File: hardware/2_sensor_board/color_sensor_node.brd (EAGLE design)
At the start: 27.9 x 30.5 mm, 19 parts, among them J1 JTAG, J2 JTAG, U1 ISL29125, U2 3.3V, U3 WS2811

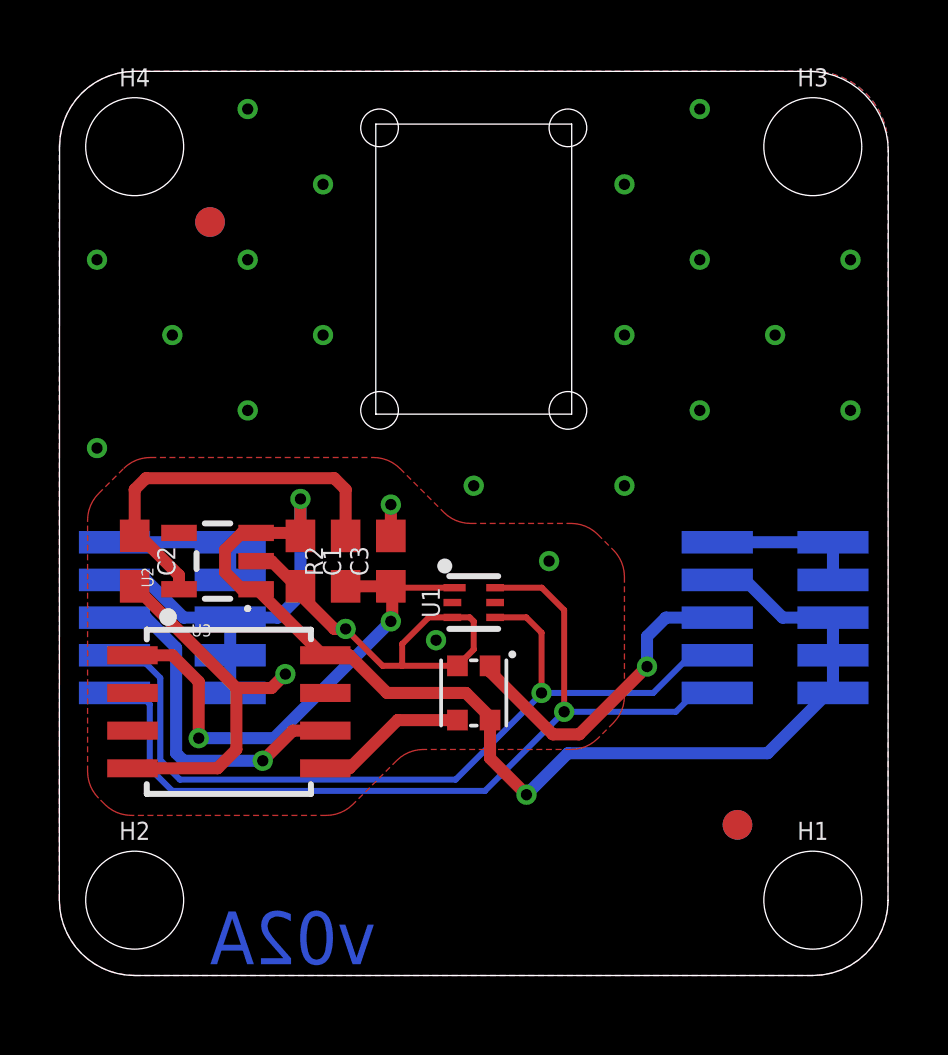
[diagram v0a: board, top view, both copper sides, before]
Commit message: increase standoff size sensor board
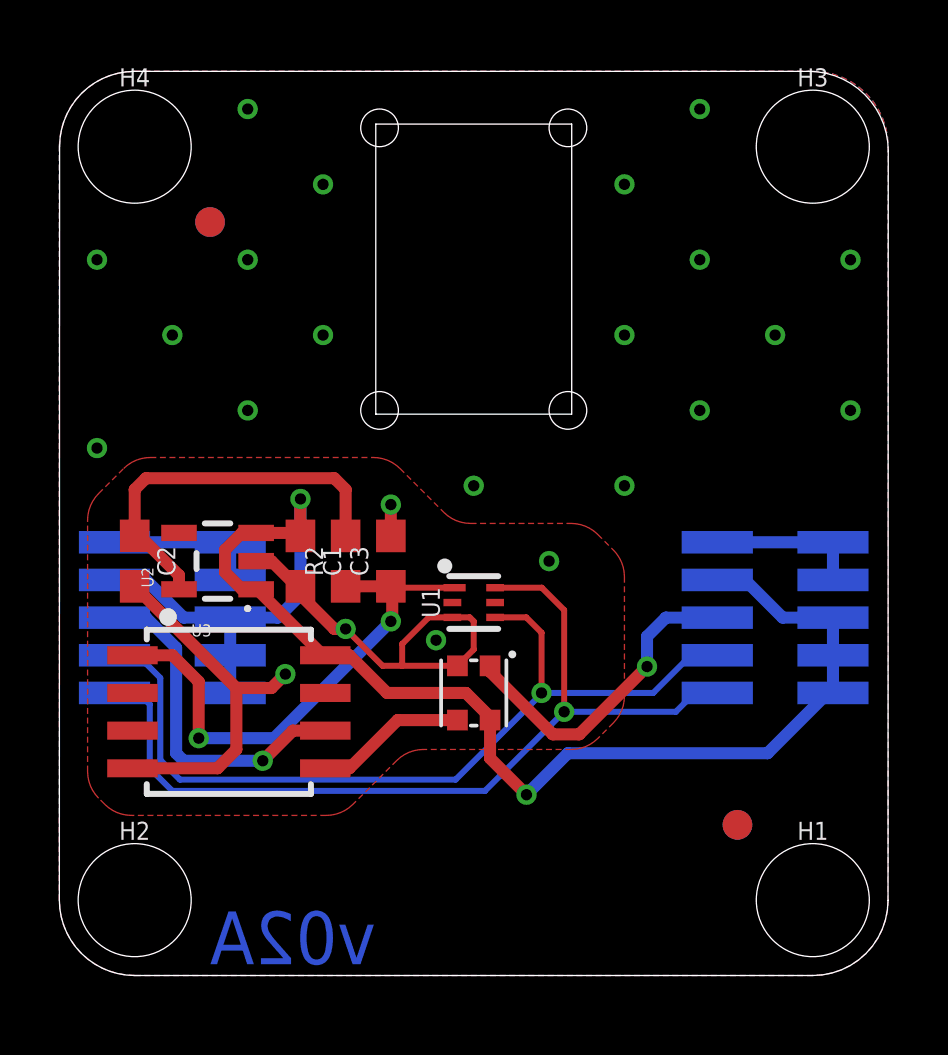
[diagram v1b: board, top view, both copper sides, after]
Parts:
- H1, H2, H3, H4: value STAND-OFF -> STAND-OFF#8; device SparkFun-Hardware:STAND-OFF -> standoff:STAND-OFF-#8
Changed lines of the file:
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@@
 <drawing>
 <settings>
-<setting alwaysvectorfont="yes"/>
+<setting alwaysvectorfont="no"/>
 <setting verticaltext="up"/>
 </settings>
-<grid distance="50" unitdist="mil" unit="mil" style="lines" multiple="1" display="yes" altdistance="1" altunitdist="mil" altunit="mil"/>
+<grid distance="5" unitdist="mil" unit="mil" style="lines" multiple="1" display="yes" altdistance="5" altunitdist="mil" altunit="mil"/>
 <layers>
 <layer number="1" name="Top" color="4" fill="1" visible="yes" active="yes"/>
-<layer number="16" name="Bottom" color="1" fill="1" visible="no" active="yes"/>
+<layer number="16" name="Bottom" color="1" fill="1" visible="yes" active="yes"/>
 <layer number="17" name="Pads" color="2" fill="1" visible="yes" active="yes"/>
 <layer number="18" name="Vias" color="2" fill="1" visible="yes" active="yes"/>
@@
 <layer number="20" name="Dimension" color="24" fill="1" visible="yes" active="yes"/>
 <layer number="21" name="tPlace" color="16" fill="1" visible="yes" active="yes"/>
-<layer number="22" name="bPlace" color="14" fill="1" visible="no" active="yes"/>
+<layer number="22" name="bPlace" color="14" fill="1" visible="yes" active="yes"/>
 <layer number="23" name="tOrigins" color="15" fill="1" visible="yes" active="yes"/>
-<layer number="24" name="bOrigins" color="15" fill="1" visible="no" active="yes"/>
-<layer number="25" name="tNames" color="7" fill="1" visible="yes" active="yes"/>
+<layer number="24" name="bOrigins" color="15" fill="1" visible="yes" active="yes"/>
+<layer number="25" name="tNames" color="7" fill="1" visible="no" active="yes"/>
 <layer number="26" name="bNames" color="7" fill="1" visible="no" active="yes"/>
 <layer number="27" name="tValues" color="7" fill="1" visible="no" active="yes"/>
@@
 <layer number="37" name="tTest" color="7" fill="1" visible="no" active="yes"/>
 <layer number="38" name="bTest" color="7" fill="1" visible="no" active="yes"/>
-<layer number="39" name="tKeepout" color="4" fill="11" visible="yes" active="yes"/>
+<layer number="39" name="tKeepout" color="4" fill="11" visible="no" active="yes"/>
 <layer number="40" name="bKeepout" color="1" fill="11" visible="no" active="yes"/>
-<layer number="41" name="tRestrict" color="4" fill="10" visible="yes" active="yes"/>
+<layer number="41" name="tRestrict" color="4" fill="10" visible="no" active="yes"/>
 <layer number="42" name="bRestrict" color="1" fill="10" visible="no" active="yes"/>
 <layer number="43" name="vRestrict" color="2" fill="10" visible="no" active="yes"/>
 <layer number="44" name="Drills" color="7" fill="1" visible="no" active="yes"/>
-<layer number="45" name="Holes" color="7" fill="1" visible="no" active="yes"/>
+<layer number="45" name="Holes" color="7" fill="1" visible="yes" active="yes"/>
 <layer number="46" name="Milling" color="3" fill="1" visible="no" active="yes"/>
 <layer number="47" name="Measures" color="7" fill="1" visible="no" active="yes"/>
@@
 <attribute name="VALUE" x="4.445" y="6.35" size="0.4064" layer="27"/>
 </element>
-<element name="H1" library="SparkFun-Hardware" package="STAND-OFF" value="STAND-OFF" x="25.4" y="2.54" smashed="yes">
+<element name="H1" library="standoff" package="STAND-OFF-#8" value="STAND-OFF#8" x="25.4" y="2.54" smashed="yes">
 <attribute name="NAME" x="25.4" y="4.572" size="0.6096" layer="25" font="vector" ratio="20" align="bottom-center"/>
 <attribute name="VALUE" x="25.4" y="0.508" size="0.6096" layer="27" font="vector" ratio="20" align="top-center"/>
 </element>
-<element name="H2" library="SparkFun-Hardware" package="STAND-OFF" value="STAND-OFF" x="2.54" y="2.54" smashed="yes">
+<element name="H2" library="standoff" package="STAND-OFF-#8" value="STAND-OFF#8" x="2.54" y="2.54" smashed="yes">
 <attribute name="NAME" x="2.54" y="4.572" size="0.6096" layer="25" font="vector" ratio="20" align="bottom-center"/>
 <attribute name="VALUE" x="2.54" y="0.508" size="0.6096" layer="27" font="vector" ratio="20" align="top-center"/>
 </element>
-<element name="H3" library="SparkFun-Hardware" package="STAND-OFF" value="STAND-OFF" x="25.4" y="27.94" smashed="yes">
+<element name="H3" library="standoff" package="STAND-OFF-#8" value="STAND-OFF#8" x="25.4" y="27.94" smashed="yes">
 <attribute name="NAME" x="25.4" y="29.972" size="0.6096" layer="25" font="vector" ratio="20" align="bottom-center"/>
 <attribute name="VALUE" x="25.4" y="25.908" size="0.6096" layer="27" font="vector" ratio="20" align="top-center"/>
 </element>
-<element name="H4" library="SparkFun-Hardware" package="STAND-OFF" value="STAND-OFF" x="2.54" y="27.94" smashed="yes">
+<element name="H4" library="standoff" package="STAND-OFF-#8" value="STAND-OFF#8" x="2.54" y="27.94" smashed="yes">
 <attribute name="NAME" x="2.54" y="29.972" size="0.6096" layer="25" font="vector" ratio="20" align="bottom-center"/>
 <attribute name="VALUE" x="2.54" y="25.908" size="0.6096" layer="27" font="vector" ratio="20" align="top-center"/>
